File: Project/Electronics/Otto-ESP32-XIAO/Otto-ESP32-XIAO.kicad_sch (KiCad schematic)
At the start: 28 parts, among them J1 Conn_01x03, J10 Conn_01x02, J11 Conn_01x04, J12 Conn_01x04, J2 Conn_01x03, J3 Conn_01x03, J4 Conn_01x03, J5 Conn_01x03, J6 Conn_01x03, J7 Conn_01x04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

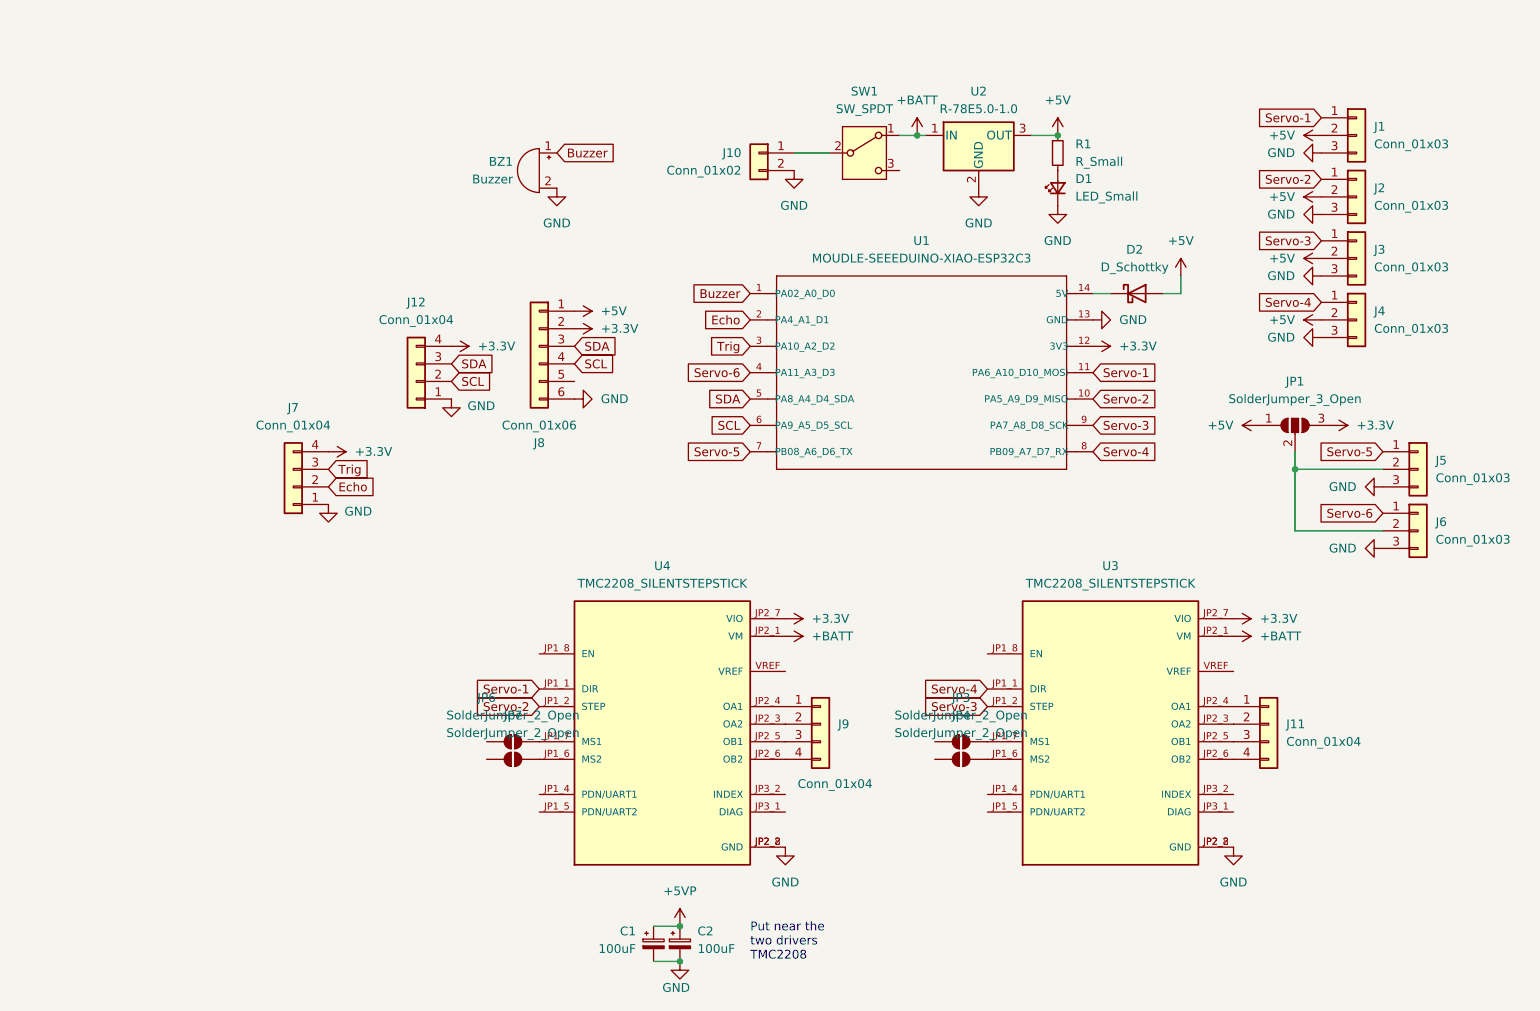
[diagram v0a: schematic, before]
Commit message: add TMC, oled and 3D models
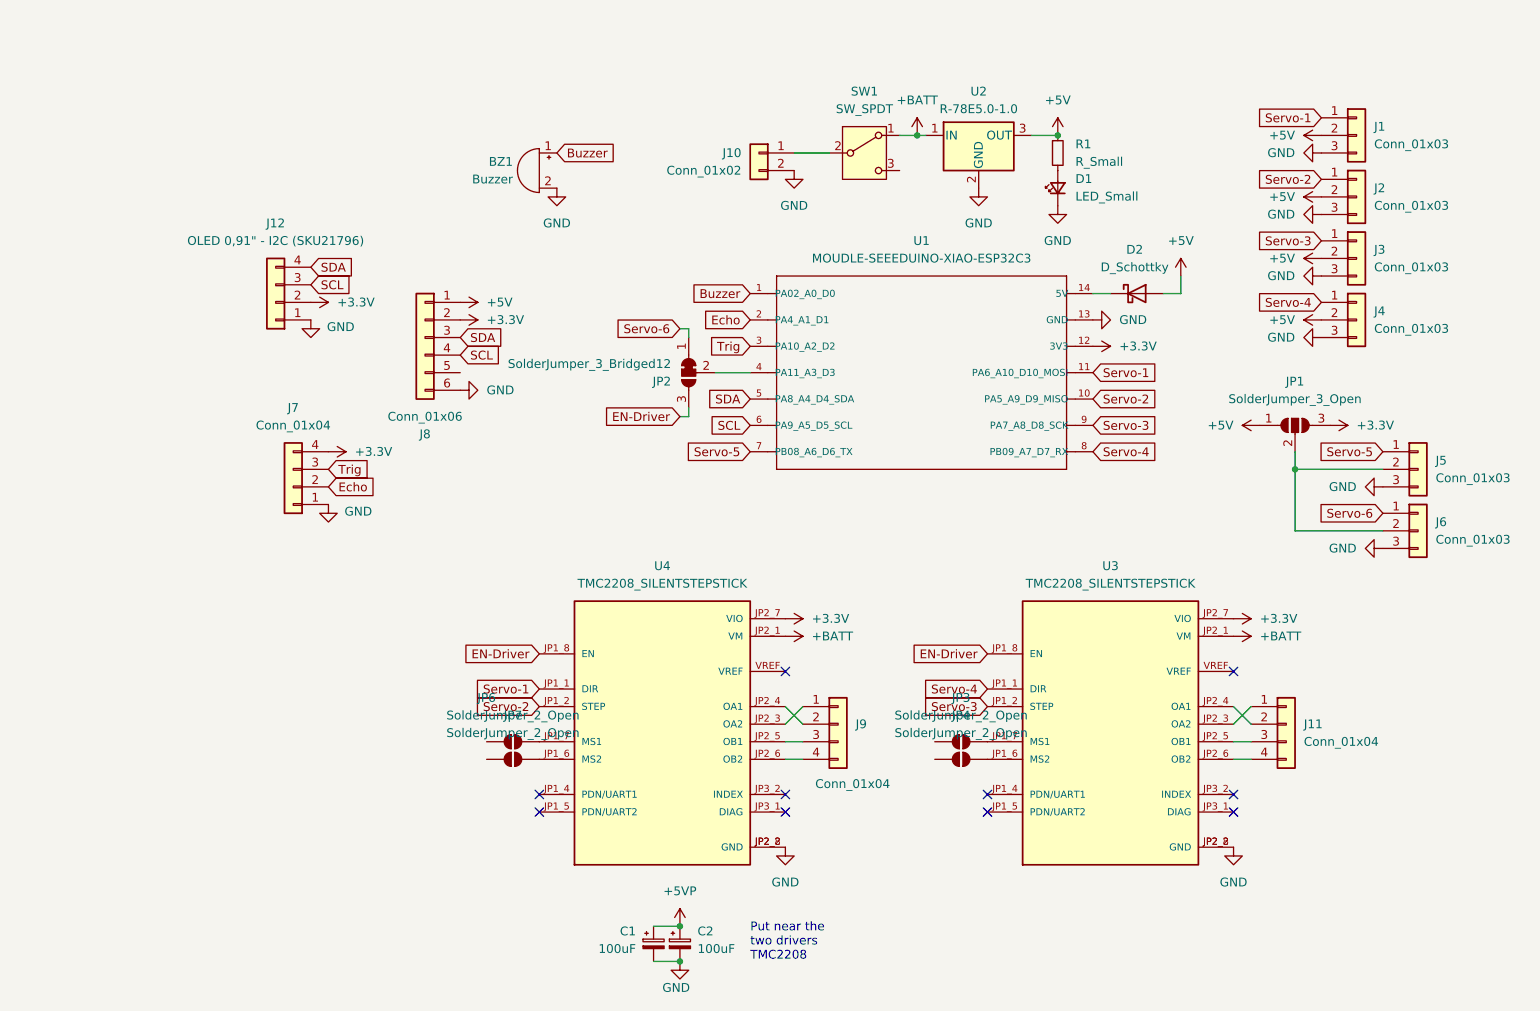
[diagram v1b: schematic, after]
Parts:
- added JP2: SolderJumper_3_Bridged12, Jumper:SolderJumper-3_P1.3mm_Bridged12_RoundedPad1.0x1.5mm, symbol Jumper:SolderJumper_3_Bridged12
- J12: value Conn_01x04 -> OLED 0,91" - I2C (SKU21796)
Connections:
- net +3.3V: now also J12.2 (Pin_2); no longer J12.4 (Pin_4)
- net SCL: now also J12.3 (Pin_3); no longer J12.2 (Pin_2)
- net SDA: now also J12.4 (Pin_4); no longer J12.3 (Pin_3)
- net Servo-6: now also JP2.1 (A); no longer U1.4 (PA11_A3_D3)
- net at J11.1 (Pin_1): now also U3.JP2_3 (OA2); no longer U3.JP2_4 (OA1)
- net at J11.2 (Pin_2): now also U3.JP2_4 (OA1); no longer U3.JP2_3 (OA2)
- net EN-Driver: now reaches U3.JP1_8 (EN)
- net EN-Driver: now also U4.JP1_8 (EN), JP2.3 (B)
- net at J9.1 (Pin_1): now also U4.JP2_3 (OA2); no longer U4.JP2_4 (OA1)
- net at J9.2 (Pin_2): now also U4.JP2_4 (OA1); no longer U4.JP2_3 (OA2)
- new net: JP2.2 (C), U1.4 (PA11_A3_D3)
- no-connect marks 0 -> 10
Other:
- moved on the sheet: J11, J8, J9

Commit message: quick update
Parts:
- removed JP2: SolderJumper_3_Bridged12, Jumper:SolderJumper-3_P1.3mm_Bridged12_RoundedPad1.0x1.5mm, symbol Jumper:SolderJumper_3_Bridged12
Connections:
- net Servo-6 is gone; now on net EN-Driver: J6.1 (Pin_1)
- net EN-Driver: now also U1.4 (PA11_A3_D3)
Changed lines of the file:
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@@
 	)
 	(junction
+		(at 114.3 88.9)
+		(diameter 0)
+		(color 0 0 0 0)
+	)
+	(junction
 		(at 200.66 102.87)
 		(diameter 0)
@@
 	(wire
 		(pts
-			(xy 113.03 95.25) (xy 113.03 93.98)
+			(xy 213.36 102.87) (xy 200.66 102.87)
 		)
 		(stroke
@@
 	(wire
 		(pts
-			(xy 213.36 102.87) (xy 200.66 102.87)
+			(xy 213.36 111.76) (xy 200.66 111.76)
 		)
 		(stroke
@@
 	(wire
 		(pts
-			(xy 213.36 111.76) (xy 200.66 111.76)
+			(xy 114.3 88.9) (xy 121.92 88.9)
 		)
 		(stroke
@@
 	(wire
 		(pts
-			(xy 111.76 82.55) (xy 113.03 82.55)
+			(xy 194.31 144.78) (xy 191.77 144.78)
 		)
 		(stroke
@@
 	(wire
 		(pts
-			(xy 194.31 144.78) (xy 191.77 144.78)
+			(xy 114.3 87.63) (xy 114.3 88.9)
 		)
 		(stroke
@@
 	(wire
 		(pts
-			(xy 200.66 102.87) (xy 200.66 100.33)
+			(xy 113.03 90.17) (xy 114.3 90.17)
 		)
 		(stroke
@@
 	(wire
 		(pts
-			(xy 127 139.7) (xy 129.54 137.16)
+			(xy 200.66 102.87) (xy 200.66 100.33)
 		)
 		(stroke
@@
 	(wire
 		(pts
-			(xy 127 137.16) (xy 129.54 139.7)
+			(xy 113.03 87.63) (xy 114.3 87.63)
 		)
 		(stroke
@@
 	(wire
 		(pts
-			(xy 116.84 88.9) (xy 121.92 88.9)
+			(xy 127 139.7) (xy 129.54 137.16)
 		)
 		(stroke
@@
 	(wire
 		(pts
-			(xy 111.76 95.25) (xy 113.03 95.25)
+			(xy 127 137.16) (xy 129.54 139.7)
 		)
 		(stroke
@@
 	(wire
 		(pts
-			(xy 200.66 111.76) (xy 200.66 102.87)
+			(xy 114.3 88.9) (xy 114.3 90.17)
 		)
 		(stroke
@@
 	(wire
 		(pts
-			(xy 191.77 137.16) (xy 194.31 139.7)
+			(xy 200.66 111.76) (xy 200.66 102.87)
 		)
 		(stroke
@@
 	(wire
 		(pts
-			(xy 113.03 82.55) (xy 113.03 83.82)
+			(xy 191.77 137.16) (xy 194.31 139.7)
 		)
 		(stroke
@@
 	(global_label "Servo-6"
 		(shape input)
-		(at 111.76 82.55 180)
+		(at 113.03 87.63 180)
 		(fields_autoplaced yes)
 		(effects
@@
 		)
 		(property "Intersheetrefs" "${INTERSHEET_REFS}"
-			(at 100.792 82.55 0)
+			(at 102.062 87.63 0)
 			(effects
 				(font
@@
 	(global_label "EN-Driver"
 		(shape input)
-		(at 111.76 95.25 180)
+		(at 113.03 90.17 180)
 		(fields_autoplaced yes)
 		(effects
@@
 		)
 		(property "Intersheetrefs" "${INTERSHEET_REFS}"
-			(at 99.2195 95.25 0)
+			(at 100.4895 90.17 0)
 			(effects
 				(font
@@
 					(unit 1)
 				)
-			)
-		)
-	)
-	(symbol
-		(lib_id "Jumper:SolderJumper_3_Bridged12")
-		(at 113.03 88.9 90)
-		(mirror x)
-		(unit 1)
-		(exclude_from_sim yes)
-		(in_bom no)
-		(on_board yes)
-		(dnp no)
-		(property "Reference" "JP2"
-			(at 110.49 90.1701 90)
-			(effects
-				(font
-					(size 1.27 1.27)
-				)
-				(justify left)
-			)
-		)
-		(property "Value" "SolderJumper_3_Bridged12"
-			(at 110.49 87.6301 90)
-			(effects
-				(font
-					(size 1.27 1.27)
-				)
-				(justify left)
-			)
-		)
-		(property "Footprint" "Jumper:SolderJumper-3_P1.3mm_Bridged12_RoundedPad1.0x1.5mm"
-			(at 113.03 88.9 0)
-			(effects
-				(font
-					(size 1.27 1.27)
-				)
-				(hide yes)
-			)
-		)
-		(property "Datasheet" "~"
-			(at 113.03 88.9 0)
-			(effects
-				(font
-					(size 1.27 1.27)
-				)
-				(hide yes)
-			)
-		)
-		(property "Description" "3-pole Solder Jumper, pins 1+2 closed/bridged"
-			(at 113.03 88.9 0)
-			(effects
-				(font
-					(size 1.27 1.27)
-				)
-				(hide yes)
-			)
-		)
-		(pin "2"
-		)
-		(pin "1"
-		)
-		(pin "3"
-		)
-		(instances
-			(project ""
-				(path "/d2682c99-4285-4c0b-9e61-08b763b3ce0d"
-					(reference "JP2")
-					(unit 1)
-				)

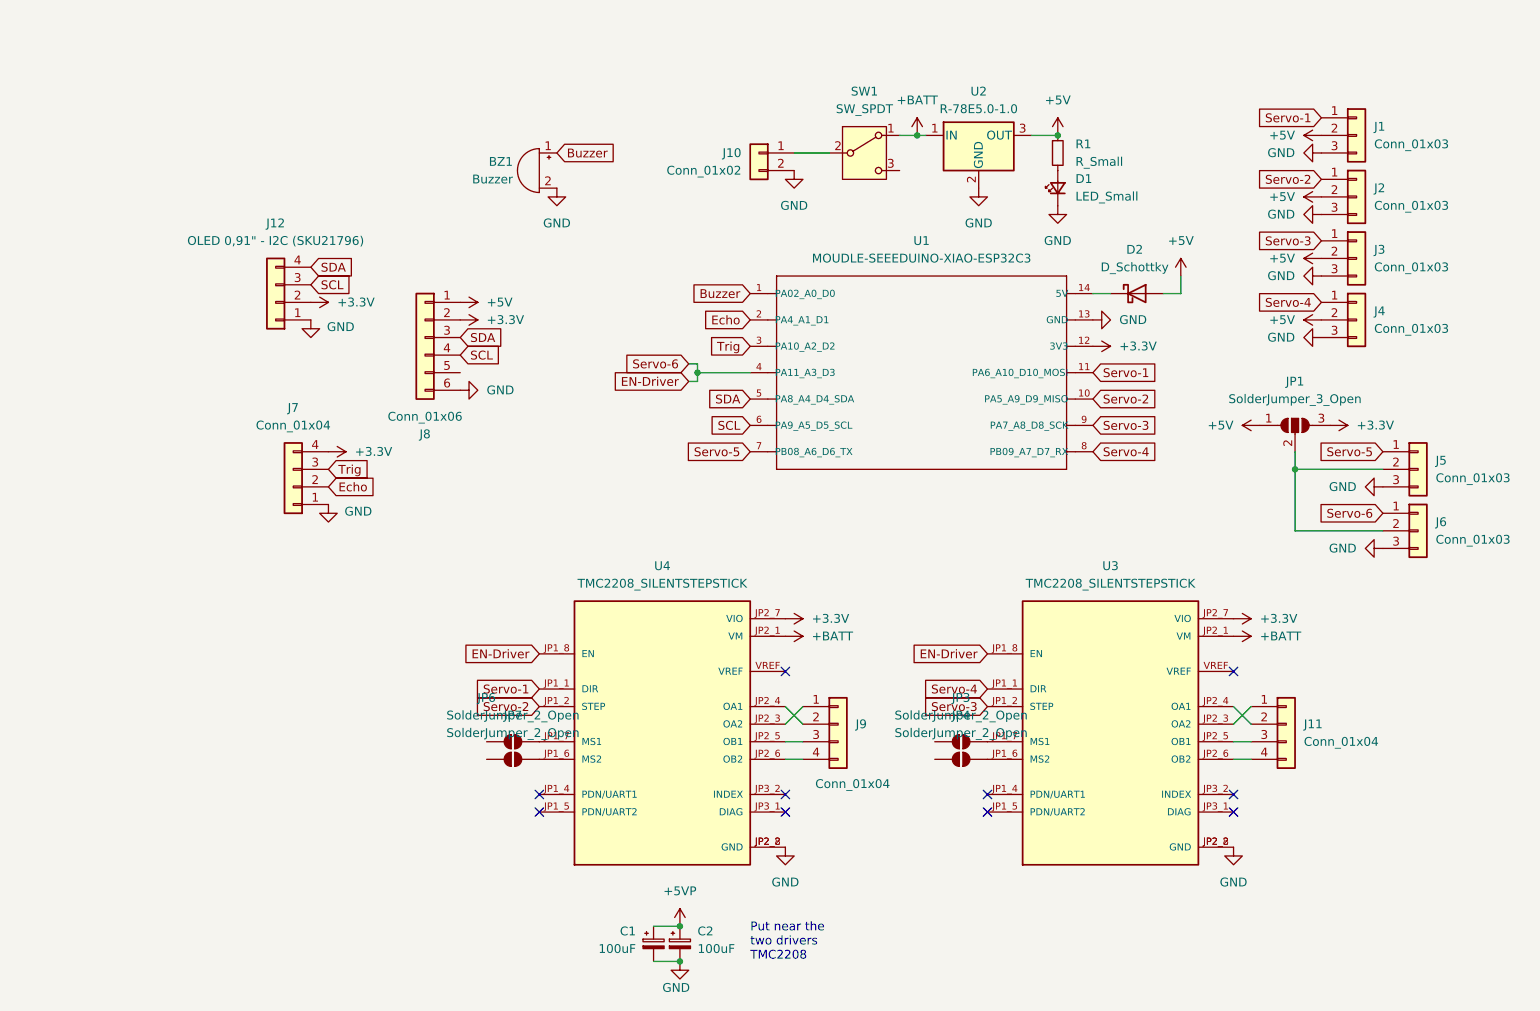
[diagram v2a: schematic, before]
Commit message: Change US sensor orientation. Add MPU6090
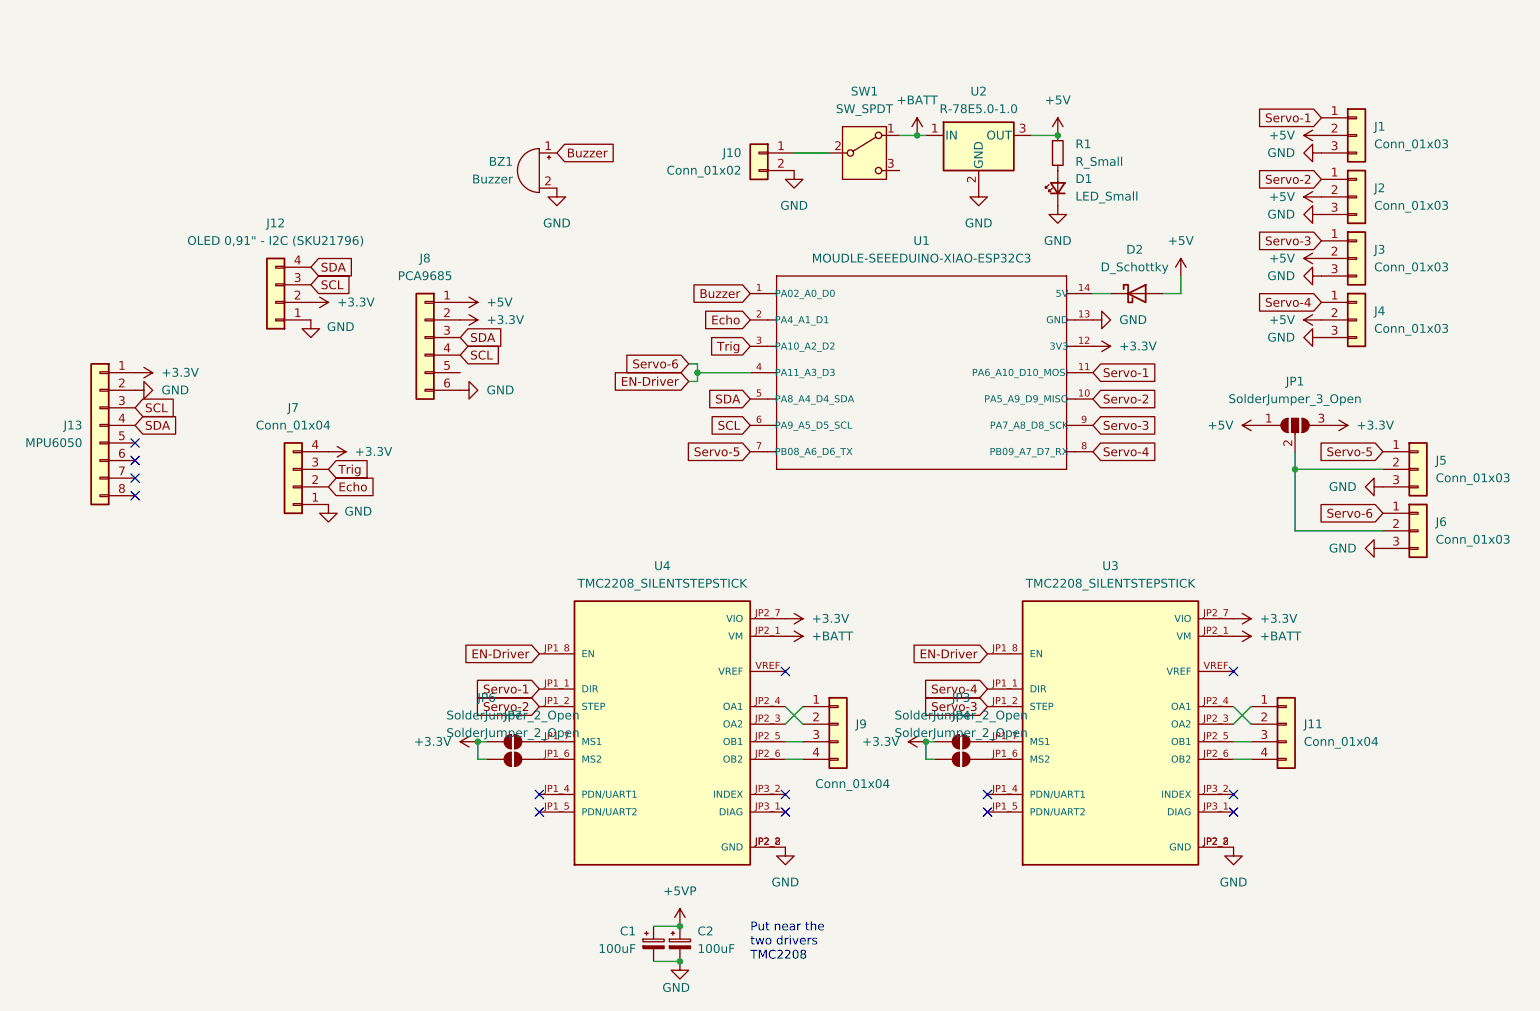
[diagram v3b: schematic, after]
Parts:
- added J13: MPU6050, Connector_PinSocket_2.54mm:PinSocket_1x08_P2.54mm_Vertical, symbol Connector_Generic:Conn_01x08
- J8: value Conn_01x06 -> PCA9685
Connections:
- net +3.3V: now also JP3.1 (A), JP4.1 (A), JP6.1 (A), JP7.1 (A), J13.1 (Pin_1)
- net GND: now also J13.2 (Pin_2)
- net SCL: now also J13.3 (Pin_3)
- net SDA: now also J13.4 (Pin_4)
- no-connect marks 10 -> 14
